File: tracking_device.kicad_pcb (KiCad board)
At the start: 4 copper layers, 74.2 x 35 mm, 105 parts, among them J1 USB_OTG, J2 CONN_COAXIAL, J3 JST-PH, J4 Micro_SD_Connector, J5 CONN_01X03, J6 CONN_01X06, J7 CONN_01X03, J8 SMA, Q1 PMGD280UN, SW1 SW_Push, U1 RClamp0503F, U2 LDK220M30R, U3 MCP73831, U4 MAX-M8, U5 STC3100, U6 STM32L476RG, U7 SX1272, U8 PE4259, Y1 ABS07-120-32.768kHz-T, Y2 Crystal

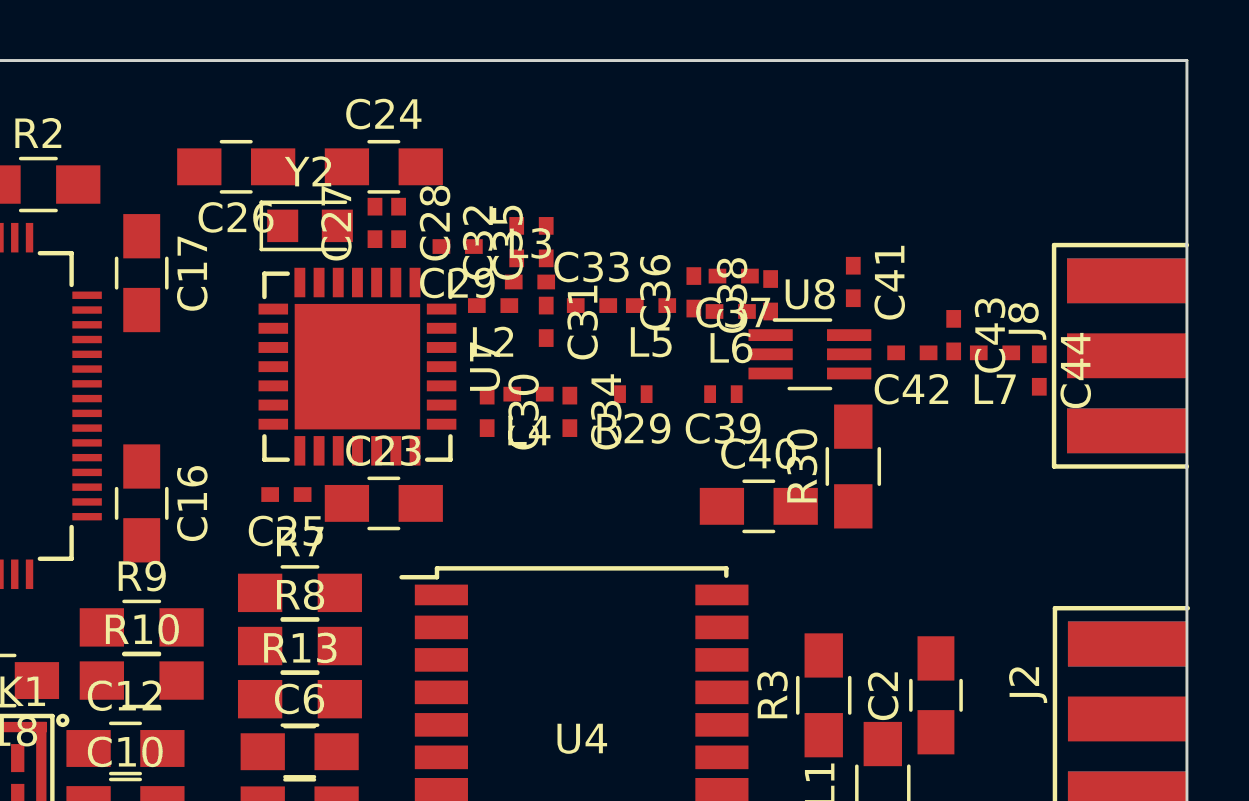
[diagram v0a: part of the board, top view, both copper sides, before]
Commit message: Added RFM95W
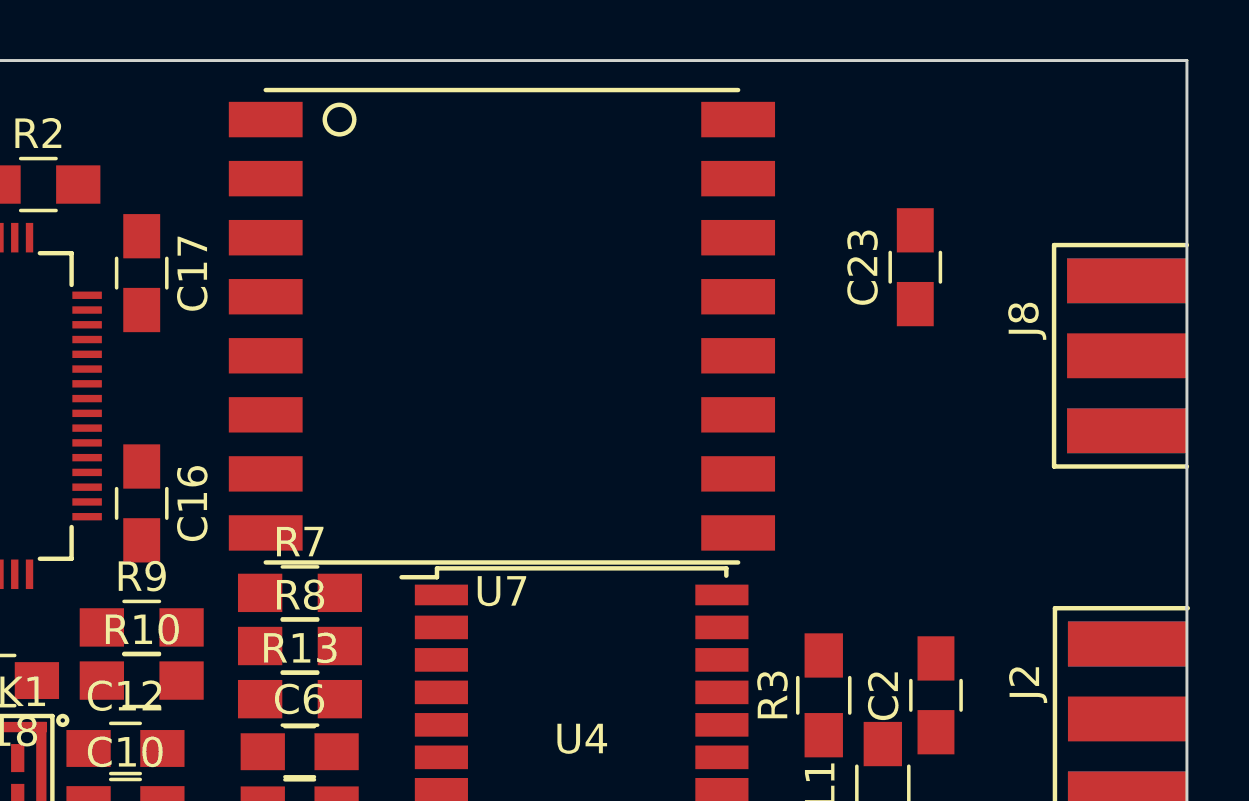
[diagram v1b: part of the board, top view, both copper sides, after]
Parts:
- removed C24, C26: 15p, Capacitors_SMD:C_0805_HandSoldering
- removed C25, C27, C28, C29, C41: 100n, Capacitors_SMD:C_0402_NoSilk
- removed C30, C43, C44: DNI, Capacitors_SMD:C_0402_NoSilk
- removed C31, C36: 8.2p, Capacitors_SMD:C_0402_NoSilk
- removed C32: 10n, Capacitors_SMD:C_0402_NoSilk
- removed C33: 22p, Capacitors_SMD:C_0402_NoSilk
- removed C34, C38: 3.3p, Capacitors_SMD:C_0402_NoSilk
- removed C35, C42: 47p, Capacitors_SMD:C_0402_NoSilk
- removed C37: 1.5n, Capacitors_SMD:C_0402_NoSilk
- removed C39: 47p, Resistors_SMD:R_0402_NoSilk
- removed C40: 1n, Capacitors_SMD:C_0805_HandSoldering
- removed L2: 2.7n, tracking_device:L_0402_NoSilk
- removed L3: 33n, tracking_device:L_0402_NoSilk
- removed L4: L, tracking_device:L_0402_NoSilk
- removed L5, L6: 5.6n, tracking_device:L_0402_NoSilk
- removed L7: 0R, tracking_device:L_0402_NoSilk
- removed R29: 0, Resistors_SMD:R_0402_NoSilk
- removed R30: 1k, Resistors_SMD:R_0805_HandSoldering
- removed U8: PE4259, tracking_device:SOT-363_SC-70-6_Handsoldering
- removed Y2: Crystal, Crystals:Crystal_SMD_2012-2pin_2.0x1.2mm_HandSoldering
- C23: value 15p -> 10u
- J6: footprint Pin_Headers:Pin_Header_Straight_1x06_Pitch2.54mm -> tracking_device:Pin_Header_Straight_1x06_Pitch2.54mm
- J7: footprint Pin_Headers:Pin_Header_Straight_1x03_Pitch2.54mm -> tracking_device:Pin_Header_Straight_1x03_Pitch2.54mm
- U7: value SX1272 -> RFM95W; footprint Housings_DFN_QFN:QFN-28-1EP_6x6mm_Pitch0.65mm -> tracking_device:RFM95W
- moved C23 19.7 mm to (157.0, 87.0), turned to 90 degrees
- moved U7 5.08 mm to (143.0, 89.0), turned to 0 degrees
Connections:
- J8 pad 1: Net-(C44-Pad1) -> Net-(J8-Pad1)
- U7 pad 1: VDD -> GND
- U7 pad 10: /SX1272/DIO1 -> GND
- U7 pad 11: /SX1272/DIO2 -> /SX1272/DIO3
- U7 pad 12: /SX1272/DIO3 -> /SX1272/DIO4
- U7 pad 13: /SX1272/DIO4 -> VDD
- U7 pad 14: /SX1272/DIO5 -> /SX1272/DIO0
- U7 pad 15: VDD -> /SX1272/DIO1
- U7 pad 16: GND -> /SX1272/DIO2
- U7 pad 2: Net-(C28-Pad2) -> /SX1272/MISO
- U7 pad 3: Net-(C27-Pad2) -> /SX1272/MOSI
- U7 pad 4: Net-(C26-Pad1) -> /Microcontroller/RADIO_SPI_SCK
- U7 pad 5: Net-(C24-Pad1) -> /SX1272/NSS
- U7 pad 7: GND -> /SX1272/DIO5
- U7 pad 9: /SX1272/DIO0 -> Net-(J8-Pad1)

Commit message: Version sent out for fabrication
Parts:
- added ?: , tracking_device:VIA_0.35mm_0.55mm, F.Cu at (97.6, 95.5)
- added ?: , tracking_device:VIA_0.35mm_0.55mm, F.Cu at (155.8, 92.2)
- added ?: , tracking_device:VIA_0.35mm_0.55mm, F.Cu at (154.3, 93.7)
- added ?: , tracking_device:VIA_0.35mm_0.55mm, F.Cu at (154.1, 94.7)
- added ?: , tracking_device:VIA_0.35mm_0.55mm, F.Cu at (153.2, 98.3)
- added ?: , tracking_device:VIA_0.35mm_0.55mm, F.Cu at (152.4, 97.7)
- added ?: , tracking_device:VIA_0.35mm_0.55mm, F.Cu at (151.5, 97.7)
- added ?: , tracking_device:VIA_0.35mm_0.55mm, F.Cu at (150.5, 97.5)
- added ?: , tracking_device:VIA_0.35mm_0.55mm, F.Cu at (149.6, 97.3)
- added ?: , tracking_device:VIA_0.35mm_0.55mm, F.Cu at (149.2, 96.4)
- added ?: , tracking_device:VIA_0.35mm_0.55mm, F.Cu at (149.1, 95.6)
- added ?: , tracking_device:VIA_0.35mm_0.55mm, F.Cu at (149.1, 94.6)
- added ?: , tracking_device:VIA_0.35mm_0.55mm, F.Cu at (155.0, 93.0)
- added ?: , tracking_device:VIA_0.35mm_0.55mm, F.Cu at (149.8, 94.0)
- added ?: , tracking_device:VIA_0.35mm_0.55mm, F.Cu at (150.0, 94.8)
- added ?: , tracking_device:VIA_0.35mm_0.55mm, F.Cu at (150.0, 95.7)
- added ?: , tracking_device:VIA_0.35mm_0.55mm, F.Cu at (150.2, 96.6)
- added ?: , tracking_device:VIA_0.35mm_0.55mm, F.Cu at (151.1, 96.9)
- added ?: , tracking_device:VIA_0.35mm_0.55mm, F.Cu at (151.9, 96.9)
- added ?: , tracking_device:VIA_0.35mm_0.55mm, F.Cu at (152.7, 96.9)
- added ?: , tracking_device:VIA_0.35mm_0.55mm, F.Cu at (155.0, 98.4)
- added ?: , tracking_device:VIA_0.35mm_0.55mm, F.Cu at (153.4, 97.5)
- added ?: , tracking_device:VIA_0.35mm_0.55mm, F.Cu at (154.2, 98.0)
- added ?: , tracking_device:VIA_0.35mm_0.55mm, F.Cu at (155.7, 93.7)
- added ?: , tracking_device:VIA_0.35mm_0.55mm, F.Cu at (155.9, 98.7)
- added ?: , tracking_device:VIA_0.35mm_0.55mm, F.Cu at (154.4, 97.1)
- added ?: , tracking_device:VIA_0.35mm_0.55mm, F.Cu at (153.9, 96.4)
- added ?: , tracking_device:VIA_0.35mm_0.55mm, F.Cu at (155.2, 97.4)
- added ?: , tracking_device:VIA_0.35mm_0.55mm, F.Cu at (104.5, 91.0)
- added ?: MOUNTING_HOLE, Mounting_Holes:MountingHole_2.2mm_M2, F.Cu at (106.1, 109.8)
- added ?: MOUNTING_HOLE, Mounting_Holes:MountingHole_2.2mm_M2, F.Cu at (142.2, 112.0)
- added ?: MOUNTING_HOLE, Mounting_Holes:MountingHole_2.2mm_M2, F.Cu at (157.0, 84.9)
- added ?: , tracking_device:VIA_0.35mm_0.55mm, F.Cu at (156.0, 97.6)
- added ?: LOGO, tracking_device:logo_2, F.Cu at (144.0, 87.1)
- added ?: , tracking_device:VIA_0.35mm_0.55mm, F.Cu at (156.1, 96.5)
- added ?: , tracking_device:VIA_0.35mm_0.55mm, F.Cu at (155.1, 96.4)
- added ?: , tracking_device:VIA_0.35mm_0.55mm, F.Cu at (156.3, 94.7)
- added ?: , tracking_device:VIA_0.35mm_0.55mm, F.Cu at (155.1, 94.7)
- added ?: , tracking_device:VIA_0.35mm_0.55mm, F.Cu at (109.4, 81.6)
- added ?: , tracking_device:VIA_0.35mm_0.55mm, F.Cu at (104.6, 83.6)
- added ?: , tracking_device:VIA_0.35mm_0.55mm, F.Cu at (103.6, 83.6)
- added ?: , tracking_device:VIA_0.35mm_0.55mm, F.Cu at (94.0, 109.8)
- added ?: , tracking_device:VIA_0.35mm_0.55mm, F.Cu at (102.6, 83.6)
- added ?: , tracking_device:VIA_0.35mm_0.55mm, F.Cu at (101.5, 84.2)
- added ?: , tracking_device:VIA_0.35mm_0.55mm, F.Cu at (100.1, 85.7)
- added ?: , tracking_device:VIA_0.35mm_0.55mm, F.Cu at (99.2, 86.3)
- added ?: , tracking_device:VIA_0.35mm_0.55mm, F.Cu at (98.3, 87.2)
- added ?: , tracking_device:VIA_0.35mm_0.55mm, F.Cu at (97.5, 88.4)
- added ?: , tracking_device:VIA_0.35mm_0.55mm, F.Cu at (97.5, 89.7)
- added ?: , tracking_device:VIA_0.35mm_0.55mm, F.Cu at (97.5, 91.2)
- added ?: , tracking_device:VIA_0.35mm_0.55mm, F.Cu at (99.7, 91.4)
- added ?: , tracking_device:VIA_0.35mm_0.55mm, F.Cu at (100.7, 91.1)
- added ?: , tracking_device:VIA_0.35mm_0.55mm, F.Cu at (159.7, 100.9)
- added ?: , tracking_device:VIA_0.35mm_0.55mm, F.Cu at (99.9, 90.5)
- added ?: , tracking_device:VIA_0.35mm_0.55mm, F.Cu at (100.8, 90.0)
- added ?: , tracking_device:VIA_0.35mm_0.55mm, F.Cu at (99.9, 89.2)
- added ?: , tracking_device:VIA_0.35mm_0.55mm, F.Cu at (101.6, 89.1)
- added ?: , tracking_device:VIA_0.35mm_0.55mm, F.Cu at (100.7, 88.4)
- added ?: , tracking_device:VIA_0.35mm_0.55mm, F.Cu at (102.5, 88.4)
- added ?: , tracking_device:VIA_0.35mm_0.55mm, F.Cu at (101.6, 87.5)
- added ?: , tracking_device:VIA_0.35mm_0.55mm, F.Cu at (103.3, 87.5)
- added ?: , tracking_device:VIA_0.35mm_0.55mm, F.Cu at (102.5, 86.6)
- added ?: , tracking_device:VIA_0.35mm_0.55mm, F.Cu at (104.0, 86.6)
- added ?: , tracking_device:VIA_0.35mm_0.55mm, F.Cu at (160.4, 100.0)
- added ?: , tracking_device:VIA_0.35mm_0.55mm, F.Cu at (103.3, 85.8)
- added ?: , tracking_device:VIA_0.35mm_0.55mm, F.Cu at (104.8, 85.8)
- added ?: , tracking_device:VIA_0.35mm_0.55mm, F.Cu at (106.5, 85.8)
- added ?: , tracking_device:VIA_0.35mm_0.55mm, F.Cu at (99.5, 82.2)
- added ?: , tracking_device:VIA_0.35mm_0.55mm, F.Cu at (93.5, 86.4)
- added ?: , tracking_device:VIA_0.35mm_0.55mm, F.Cu at (93.9, 81.1)
- added ?: , tracking_device:VIA_0.35mm_0.55mm, F.Cu at (94.0, 106.0)
- added ?: , tracking_device:VIA_0.35mm_0.55mm, F.Cu at (138.8, 81.3)
- added ?: , tracking_device:VIA_0.35mm_0.55mm, F.Cu at (146.6, 82.4)
- added ?: , tracking_device:VIA_0.35mm_0.55mm, F.Cu at (149.1, 80.9)
- added ?: , tracking_device:VIA_0.35mm_0.55mm, F.Cu at (158.8, 100.0)
- added ?: , tracking_device:VIA_0.35mm_0.55mm, F.Cu at (145.3, 84.7)
- added ?: , tracking_device:VIA_0.35mm_0.55mm, F.Cu at (142.5, 86.1)
- added ?: , tracking_device:VIA_0.35mm_0.55mm, F.Cu at (140.0, 84.6)
- added ?: , tracking_device:VIA_0.35mm_0.55mm, F.Cu at (114.7, 91.9)
- added ?: , tracking_device:VIA_0.35mm_0.55mm, F.Cu at (108.2, 89.3)
- added ?: , tracking_device:VIA_0.35mm_0.55mm, F.Cu at (108.2, 91.1)
- added ?: , tracking_device:VIA_0.35mm_0.55mm, F.Cu at (108.2, 87.6)
- added ?: , tracking_device:VIA_0.35mm_0.55mm, F.Cu at (102.2, 113.3)
- added ?: , tracking_device:VIA_0.35mm_0.55mm, F.Cu at (140.9, 109.2)
- added ?: , tracking_device:VIA_0.35mm_0.55mm, F.Cu at (144.0, 114.0)
- added ?: , tracking_device:VIA_0.35mm_0.55mm, F.Cu at (157.0, 100.0)
- added ?: , tracking_device:VIA_0.35mm_0.55mm, F.Cu at (139.1, 114.0)
- added ?: , tracking_device:VIA_0.35mm_0.55mm, F.Cu at (143.4, 106.4)
- added ?: , tracking_device:VIA_0.35mm_0.55mm, F.Cu at (145.9, 102.1)
- added ?: , tracking_device:VIA_0.35mm_0.55mm, F.Cu at (145.6, 98.9)
- added ?: , tracking_device:VIA_0.35mm_0.55mm, F.Cu at (145.6, 96.3)
- added ?: , tracking_device:VIA_0.35mm_0.55mm, F.Cu at (148.3, 89.9)
- added ?: , tracking_device:VIA_0.35mm_0.55mm, F.Cu at (150.1, 87.9)
- added ?: , tracking_device:VIA_0.35mm_0.55mm, F.Cu at (154.2, 92.2)
- added ?: , tracking_device:VIA_0.35mm_0.55mm, F.Cu at (153.8, 109.6)
- added ?: , tracking_device:VIA_0.35mm_0.55mm, F.Cu at (150.3, 109.7)
- added ?: , tracking_device:VIA_0.35mm_0.55mm, F.Cu at (159.7, 90.5)
- added ?: , tracking_device:VIA_0.35mm_0.55mm, F.Cu at (160.4, 111.8)
- added ?: , tracking_device:VIA_0.35mm_0.55mm, F.Cu at (160.0, 110.5)
- added ?: , tracking_device:VIA_0.35mm_0.55mm, F.Cu at (157.2, 110.4)
- added ?: , tracking_device:VIA_0.35mm_0.55mm, F.Cu at (160.5, 101.9)
- added ?: , tracking_device:VIA_0.35mm_0.55mm, F.Cu at (158.8, 101.7)
- added ?: , tracking_device:VIA_0.35mm_0.55mm, F.Cu at (157.8, 100.9)
- added ?: , tracking_device:VIA_0.35mm_0.55mm, F.Cu at (156.9, 101.8)
- added ?: , tracking_device:VIA_0.35mm_0.55mm, F.Cu at (155.7, 109.3)
- added ?: , tracking_device:VIA_0.35mm_0.55mm, F.Cu at (155.7, 108.4)
- added ?: , tracking_device:VIA_0.35mm_0.55mm, F.Cu at (146.6, 107.0)
- added ?: , tracking_device:VIA_0.35mm_0.55mm, F.Cu at (160.4, 91.2)
- added ?: , tracking_device:VIA_0.35mm_0.55mm, F.Cu at (146.7, 105.3)
- added ?: , tracking_device:VIA_0.35mm_0.55mm, F.Cu at (146.9, 106.1)
- added ?: , tracking_device:VIA_0.35mm_0.55mm, F.Cu at (150.3, 108.0)
- added ?: , tracking_device:VIA_0.35mm_0.55mm, F.Cu at (152.0, 108.0)
- added ?: , tracking_device:VIA_0.35mm_0.55mm, F.Cu at (154.7, 108.0)
- added ?: , tracking_device:VIA_0.35mm_0.55mm, F.Cu at (155.5, 107.5)
- added ?: , tracking_device:VIA_0.35mm_0.55mm, F.Cu at (151.2, 107.5)
- added ?: , tracking_device:VIA_0.35mm_0.55mm, F.Cu at (150.4, 106.9)
- added ?: , tracking_device:VIA_0.35mm_0.55mm, F.Cu at (152.0, 106.9)
- added ?: , tracking_device:VIA_0.35mm_0.55mm, F.Cu at (152.9, 107.5)
- added ?: , tracking_device:VIA_0.35mm_0.55mm, F.Cu at (159.1, 91.2)
- added ?: , tracking_device:VIA_0.35mm_0.55mm, F.Cu at (153.3, 104.7)
- added ?: , tracking_device:VIA_0.35mm_0.55mm, F.Cu at (153.9, 107.5)
- added ?: , tracking_device:VIA_0.35mm_0.55mm, F.Cu at (154.8, 106.9)
- added ?: , tracking_device:VIA_0.35mm_0.55mm, F.Cu at (156.1, 106.9)
- added ?: , tracking_device:VIA_0.35mm_0.55mm, F.Cu at (155.3, 104.7)
- added ?: , tracking_device:VIA_0.35mm_0.55mm, F.Cu at (156.1, 105.3)
- added ?: , tracking_device:VIA_0.35mm_0.55mm, F.Cu at (154.6, 105.3)
- added ?: , tracking_device:VIA_0.35mm_0.55mm, F.Cu at (151.2, 104.8)
- added ?: , tracking_device:VIA_0.35mm_0.55mm, F.Cu at (152.0, 105.3)
- added ?: , tracking_device:VIA_0.35mm_0.55mm, F.Cu at (150.4, 105.3)
- added J4: CONN_01X02, tracking_device:Pin_Header_Straight_2x01_Pitch2.54mm, F.Cu at (147.4, 95.1)
- added J6: CONN_01X02, tracking_device:Pin_Header_Straight_2x01_Pitch2.54mm, F.Cu at (97.2, 110.7)
- added J7: JST-PH, tracking_device:JST_PH_S2B-PH-SM4-TB_02x2.00mm_Angled, F.Cu at (93.2, 106.6)
- added R4: 10k, Resistors_SMD:R_0805_HandSoldering, F.Cu at (118.2, 110.4)
- added R5: 5.6k, Resistors_SMD:R_0805_HandSoldering, F.Cu at (120.0, 110.4)
- added SW1: SW_SPDT, tracking_device:CSS-1210TB, F.Cu at (124.6, 111.5)
- added SW2: SW_SPDT, tracking_device:CSS-1210TB, F.Cu at (134.0, 111.5)
- added TP1: TEST, Measurement_Points:Measurement_Point_Round-TH_Small, F.Cu at (94.4, 90.8)
- added TP10: TEST, Measurement_Points:Measurement_Point_Round-TH_Small, F.Cu at (96.0, 85.2)
- added TP11: TEST, Measurement_Points:Measurement_Point_Round-TH_Small, F.Cu at (96.0, 82.5)
- added TP2: TEST, Measurement_Points:Measurement_Point_Round-TH_Small, F.Cu at (141.9, 82.0)
- added TP3: TEST, Measurement_Points:Measurement_Point_Round-TH_Small, F.Cu at (139.1, 109.7)
- added TP4: TEST, Measurement_Points:Measurement_Point_Round-TH_Small, F.Cu at (139.0, 112.1)
- added TP5: TEST, Measurement_Points:Measurement_Point_Round-TH_Small, F.Cu at (144.8, 82.0)
- added TP6: TEST, Measurement_Points:Measurement_Point_Round-TH_Small, F.Cu at (94.4, 88.0)
- added TP7: TEST, Measurement_Points:Measurement_Point_Round-TH_Small, F.Cu at (128.6, 112.4)
- added TP8: TEST, Measurement_Points:Measurement_Point_Round-TH_Small, F.Cu at (128.6, 110.2)
- added TP9: TEST, Measurement_Points:Measurement_Point_Round-TH_Small, F.Cu at (102.6, 108.8)
- J3: value JST-PH -> CONN_01X02; footprint Connectors_JST:JST_PH_S2B-PH-SM4-TB_02x2.00mm_Angled -> tracking_device:Pin_Header_Straight_2x01_Pitch2.54mm
- J5: value CONN_01X03 -> CONN_01X02; footprint Pin_Headers:Pin_Header_Straight_1x03_Pitch2.54mm -> tracking_device:Pin_Header_Straight_2x01_Pitch2.54mm
- R12: renamed from R5; value 100 -> 100 (DNI)
- R14: renamed from R6; value 10k -> 10k (DNI)
- R15: renamed from R12; value 12 -> DNI
- R16: renamed from R14; value 500k -> 12k
- U5: footprint Housings_SSOP:MSOP-8_3x3mm_Pitch0.65mm -> Housings_DFN_QFN:DFN-8-1EP_3x3mm_Pitch0.5mm
- moved R30 45.4 mm to (152.4, 111.6)
- moved D3 41.7 mm to (152.4, 113.6), turned to 180 degrees
- moved R29 39.9 mm to (147.2, 111.6), turned to 180 degrees
- moved J10 37.6 mm to (127.7, 82.0)
- moved J3 37.5 mm to (135.2, 113.0), turned to 180 degrees
- moved J9 37.5 mm to (111.2, 82.0)
- moved SW3 37.5 mm to (154.7, 88.2), turned to 90 degrees
- moved D2 36.2 mm to (147.2, 113.6), turned to 180 degrees
- moved J5 32.3 mm to (126.0, 113.0), turned to 180 degrees
- moved R27 11.2 mm to (157.2, 111.6)
- moved R23 9.61 mm to (112.0, 84.8)
- moved R11 9.31 mm to (129.8, 108.0), turned to 0 degrees
- moved R18 8.41 mm to (112.0, 93.8)
- moved J11 7.64 mm to (161.0, 95.6)
- moved C1 7.52 mm to (118.4, 105.8), turned to 270 degrees
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- renumbered C11 to C10, C10 to C11, J7 to J10, J8 to J11, J4 to J8, J6 to J9, R3 to R1, R15 to R17, R16 to R18, R17 to R19, R1 to R2, R18 to R20, R19 to R21, R20 to R22, R21 to R23, R22 to R24, R23 to R25, R24 to R26, R25 to R27, R26 to R28, R27 to R29, R2 to R3, R28 to R30, R4 to R6, SW1 to SW3, U4 to U3, U3 to U4
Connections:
- C1 pad 1: /VBAT -> GND
- C1 pad 2: GND -> /VBAT
- J3 pad 1: /VBAT -> /GPS_I2C_SCL
- J3 pad 2: Net-(J3-Pad2) -> /GPS_I2C_SDA
- J5 pad 1: VDD -> /PMIC_I2C_SCL
- J5 pad 2: Net-(J5-Pad2) -> /PMIC_I2C_SDA
- Q1 pad 1: Net-(Q1-Pad1) -> GND
- R15 pad 1: GND -> Net-(Q1-Pad3)
- R15 pad 2: Net-(Q1-Pad1) -> Net-(R15-Pad2)
- R16 pad 1: Net-(Q1-Pad3) -> Net-(R15-Pad2)
- R25 pad 1: Net-(J3-Pad2) -> Net-(J6-Pad2)
- R26 pad 2: Net-(J5-Pad2) -> Net-(R26-Pad2)
- R27 pad 1: Net-(J5-Pad2) -> Net-(R26-Pad2)
- R28 pad 1: Net-(J5-Pad2) -> Net-(R26-Pad2)
- U3 pad 4: /GPS_EXTINT -> /GPS_TIMEPULSE
- U4 pad 5: Net-(Q1-Pad3) -> Net-(R15-Pad2)
- U5 pad 6: Net-(J3-Pad2) -> Net-(J6-Pad2)
- U6 pad 11: Net-(U6-Pad11) -> /Microcontroller/SWITCH_1
- U6 pad 17: Net-(U6-Pad17) -> /Microcontroller/SWITCH_2
- U6 pad 26: /PMIC_FAST -> Net-(U6-Pad26)
- U6 pad 28: Net-(U6-Pad28) -> /GPS_EXTINT
- U6 pad 33: Net-(U6-Pad33) -> /VUSB_DET
- U6 pad 36: Net-(U6-Pad36) -> /GPS_TIMEPULSE
- U6 pad 42: Net-(U6-Pad42) -> /PMIC_FAST
- U6 pad 56: Net-(U6-Pad56) -> /GPS_RESET_N
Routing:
- net /GPS_RESET_N: track 0.00 -> 60.4 mm, vias 0 -> 4
- net /Microcontroller/NRST: track 0.00 -> 59.0 mm, vias 0 -> 4
- net /PMIC_STAT: track 0.00 -> 57.3 mm, vias 0 -> 3
- net /PMIC_FAST: track 2.10 -> 54.5 mm, vias 0 -> 3
- net VDD: track 0.00 -> 48.3 mm, vias 0 -> 24
- net /PMIC_I2C_SCL: track 0.00 -> 48.3 mm, vias 0 -> 2
- net /GPS_I2C_SCL: track 0.00 -> 47.0 mm, vias 0 -> 8
- net Net-(R15-Pad2): track 0.00 -> 46.7 mm, vias 0 -> 3
- net /LSE_CLK: track 0.00 -> 46.5 mm, vias 0 -> 4
- net GND: track 0.00 -> 44.7 mm, vias 0 -> 65
- net /SX1272/DIO1: track 0.00 -> 44.2 mm, vias 0 -> 2
- net /USB_ID: track 6.30 -> 49.3 mm
- net /VUSB: track 15.0 -> 57.9 mm, vias 0 -> 4
- net /GPS_TIMEPULSE: track 0.00 -> 42.2 mm, vias 0 -> 4
- net /SX1272/DIO0: track 0.00 -> 41.7 mm, vias 0 -> 2
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- added copper zone on B.Cu, net GND
- added copper zone on F.Cu, net GND
- added copper zone on Ground, net GND
- added copper zone on Power, net VDD
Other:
- board size 74.2 x 35 mm -> 68.9 x 35 mm
- net class 50 ohm: clearance 0.2 -> 0.16
- net class Default: clearance 0.25 -> 0.16
- net class USB: clearance 0.15 -> 0.16
- net class power: clearance 0.3 -> 0.16
- rule trace_clearance: 0.25 -> 0.16
- board text added: "Spy Thing Nov 8 2017"

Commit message: Working on rev 3, started board layout
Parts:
- removed ? (x125): , tracking_device:VIA_0.35mm_0.55mm
- removed ?: LOGO, tracking_device:logo_2
- removed the C2 at (155.2, 101.7)
- removed the C8 at (134.6, 108.0)
- removed J11: SMA, tracking_device:RP-SMA
- removed the J2 at (161.0, 106.2)
- removed the J7 at (93.2, 106.6)
- removed the R1 at (151.3, 101.7)
- removed the R11 at (129.8, 108.0)
- removed the R12 at (112.0, 100.6)
- removed the R13 at (134.6, 102.0)
- removed the R14 at (107.4, 103.2)
- removed the R2 at (126.3, 84.8)
- removed R26: 10k, Resistors_SMD:R_0805_HandSoldering
- removed R27: DNI, Resistors_SMD:R_0805_HandSoldering
- removed R28: 0, Resistors_SMD:R_0805_HandSoldering
- removed the R3 at (131.3, 84.8)
- removed the R4 at (118.2, 110.4)
- removed the R5 at (120.0, 110.4)
- removed the R6 at (107.0, 99.8)
- removed the TP6 at (94.4, 88.0)
- removed the U3 at (143.8, 102.8)
- added C13: 100n, Capacitors_SMD:C_0805_HandSoldering, F.Cu at (99.7, 125.0)
- added C22: 10u, Capacitors_SMD:C_0805_HandSoldering, F.Cu at (122.0, 56.8)
- added C23: 10u, Capacitors_SMD:C_0805_HandSoldering, F.Cu at (115.5, 56.8)
- added J5: CONN_01X02, tracking_device:Pin_Header_Straight_2x01_Pitch2.54mm, F.Cu at (127.0, 125.1)
- added R15: 10k, Resistors_SMD:R_0805_HandSoldering, F.Cu at (108.8, 125.1)
- added U5: REG113NA-3.3, tracking_device:SOT-23-5_HandSoldering, B.Cu at (131.2, 58.0)
- C11: renamed from C1; value 1u -> 100n; moved to B.Cu
- C12: renamed from C4; value 1u -> 4.7u; moved to B.Cu
- C3, J1, U1, U6: moved to B.Cu
- C4: renamed from C5; moved to B.Cu
- C5: renamed from C9; moved to B.Cu
- C6: renamed from C10; moved to B.Cu
- D1: value 5.6V Zener -> NSR0320MW2T1G; footprint tracking_device:DO-214AC -> Diodes_SMD:D_SOD-323_HandSoldering
- J6: value CONN_01X02 -> JST-PH; footprint tracking_device:Pin_Header_Straight_2x01_Pitch2.54mm -> tracking_device:PH-2AWD; moved to B.Cu
- J7: renamed from J8; moved to B.Cu
- L1: value 27n -> L
- Q1: value PMGD280UN -> Si2343DS; footprint tracking_device:SOT-363_SC-70-6_Handsoldering -> TO_SOT_Packages_SMD:SOT-23_Handsoldering; moved to B.Cu
- R10: renamed from R19; moved to B.Cu
- R11: renamed from R20; moved to B.Cu
- R12: renamed from R21; moved to B.Cu
- R13: renamed from R22; moved to B.Cu
- R14: renamed from R23; moved to B.Cu
- R16: value 12k -> 10k
- R5: renamed from R15; value DNI -> 12k; moved to B.Cu
- R6: renamed from R17; moved to B.Cu
- R7: renamed from R24; moved to B.Cu
- R8: renamed from R25; moved to B.Cu
- R9: renamed from R18; moved to B.Cu
- SW1, SW2: value SW_SPDT -> PUSH; footprint tracking_device:CSS-1210TB -> tracking_device:K2-1102SP-I4SC-04
- U2: value LDK220M30R -> SAM-M8; footprint tracking_device:SOT-23-5_HandSoldering -> tracking_device:SAM-M8
- U3: renamed from U4; moved to B.Cu
- U4: renamed from U5; moved to B.Cu
- moved U2 93.2 mm to (197.5, 65.2), turned to 0 degrees
- moved SW2 92.3 mm to (184.2, 34.1)
- moved SW1 90.7 mm to (172.1, 34.1)
- moved C7 88.8 mm to (168.4, 26.0)
- moved C8 88.8 mm to (168.4, 24.0)
- moved MK1 88.3 mm to (163.2, 25.4)
- moved C10 85.3 mm to (172.4, 43.6)
- moved C9 85.3 mm to (167.4, 43.6)
- moved R1 84.9 mm to (208.1, 69.2), turned to 180 degrees
- moved R4 84.9 mm to (208.1, 67.2), turned to 180 degrees
- moved R2 81.3 mm to (208.1, 63.2), turned to 180 degrees
- moved R3 81.3 mm to (208.1, 65.2), turned to 180 degrees
- moved C14 78.9 mm to (125.5, 26.9)
- moved C18 78.9 mm to (123.8, 26.9)
- moved Y1 78.9 mm to (123.7, 23.4)
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- gave numbers to parts that had none: 3
- renumbered C6 to C1, C14 to C10, C15 to C14, C16 to C15, C17 to C16, C18 to C17, C19 to C18, C20 to C19, C7 to C2, C21 to C20, C22 to C21, C23 to C24, C11 to C7, C12 to C8, C13 to C9, J3 to J2, J4 to J3, J5 to J4, J9 to J8, J10 to J9, R10 to R1, R29 to R17, R30 to R18, R7 to R2, R8 to R3, R9 to R4, TP11 to TP10, TP5 to TP2, TP4 to TP3, TP3 to TP4, TP2 to TP5, TP7 to TP6, TP8 to TP7, TP9 to TP8, TP10 to TP9
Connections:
- C11 pad 2: /VBAT -> Net-(C11-Pad2)
- C24 pad 2: GND -> /SX1272/RADIO_GND
- C5 pad 1: Net-(C9-Pad1) -> Net-(C5-Pad1)
- D1 pad 1: Net-(C9-Pad1) -> Net-(C11-Pad2)
- D1 pad 2: GND -> /VUSB
- L1 pad 1: /GPS_ANT -> /SX1272/ANTENNA
- L1 pad 2: Net-(C2-Pad1) -> Net-(C22-Pad1)
- Q1 pad 1: GND -> /VUSB
- Q1 pad 2: Net-(Q1-Pad2) -> Net-(C11-Pad2)
- Q1 pad 3: Net-(Q1-Pad3) -> /VBAT
- R1 pad 2: Net-(R10-Pad2) -> Net-(R1-Pad2)
- R16 pad 1: Net-(R15-Pad2) -> VDD
- R16 pad 2: GND -> /Microcontroller/NRST
- R2 pad 1: /GPS_UART_TX -> /GPS_UART_RX
- R2 pad 2: Net-(R7-Pad2) -> Net-(R2-Pad2)
- R3 pad 1: /GPS_UART_RX -> /GPS_UART_TX
- R3 pad 2: Net-(R8-Pad2) -> Net-(R3-Pad2)
- R4 pad 2: Net-(R9-Pad2) -> Net-(R4-Pad2)
- R5 pad 1: Net-(Q1-Pad3) -> GND
- R5 pad 2: Net-(R15-Pad2) -> Net-(R5-Pad2)
- R6 pad 2: Net-(C9-Pad1) -> Net-(C5-Pad1)
- SW1 pad 1: VDD -> /Microcontroller/SWITCH_1
- SW1 pad 2: /Microcontroller/SWITCH_1 -> GND
- SW2 pad 1: VDD -> /Microcontroller/SWITCH_2
- SW2 pad 2: /Microcontroller/SWITCH_2 -> GND
- TP5 pad 1: /VUSB_DET -> /VUSB
- U2 pad 1: /VBAT -> VDD
- U2 pad 2: GND -> VDD
- U2 pad 3: /VBAT -> VDD
- U2 pad 4: Net-(R4-Pad1) -> GND
- U2 pad 5: VDD -> GND
- U3 pad 5: Net-(R15-Pad2) -> Net-(R5-Pad2)
- U4 pad 8: Net-(C9-Pad1) -> Net-(C5-Pad1)
- U6 pad 33: /VUSB_DET -> /VUSB
- U6 pad 60: Net-(R26-Pad1) -> GND
- U7 pad 1: GND -> /SX1272/RADIO_GND
- U7 pad 10: GND -> /SX1272/RADIO_GND
- U7 pad 8: GND -> /SX1272/RADIO_GND
- U7 pad 9: Net-(J11-Pad1) -> Net-(C22-Pad1)
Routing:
- net (no net): track 0.00 -> 1288.5 mm, vias 0 -> 176
- net Net-(R15-Pad2): track 46.7 -> 0.00 mm, vias 3 -> 0
- net /VBAT: track 44.9 -> 0.00 mm, vias 5 -> 0
- net /SX1272/DIO1: track 44.2 -> 0.00 mm, vias 2 -> 0
- net /USB_ID: track 49.3 -> 5.12 mm, vias 2 -> 1
- net /PMIC_I2C_SCL: track 48.3 -> 4.33 mm, vias 2 -> 0
- net /SX1272/DIO0: track 41.7 -> 0.00 mm, vias 2 -> 0
- net /PMIC_I2C_SDA: track 41.2 -> 0.00 mm, vias 3 -> 0
- net /USB_D-: track 40.2 -> 1.62 mm, vias 2 -> 1
- net Net-(R26-Pad1): track 38.5 -> 0.00 mm, vias 2 -> 0
- net /USB_D+: track 39.5 -> 3.19 mm, vias 2 -> 1
- net GND: track 44.7 -> 9.79 mm, vias 65 -> 7
- net VDD: track 48.3 -> 14.0 mm, vias 24 -> 6
- net /SX1272/DIO4: track 29.8 -> 0.00 mm, vias 2 -> 0
- net /SX1272/MOSI: track 29.1 -> 0.00 mm, vias 2 -> 0
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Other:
- board size 68.9 x 35 mm -> 68.9 x 77 mm
